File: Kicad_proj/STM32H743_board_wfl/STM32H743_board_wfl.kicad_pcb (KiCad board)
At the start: 4 copper layers, 38.5 x 38.5 mm, 4 parts

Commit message: PCB v0.1b connectors
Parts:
- removed REF** (x4): MountingHole_4mm, MountingHole:MountingHole_4mm
- added C1: 47uF, Capacitor_SMD:C_1206_3216Metric, F.Cu at (192.0, 115.7)
- added C10: 1uF, Capacitor_SMD:C_0603_1608Metric, F.Cu at (191.2, 101.2)
- added C11: 4.7uF, Capacitor_SMD:C_0603_1608Metric, F.Cu at (191.2, 103.7)
- added C12: 4.7uF, Capacitor_SMD:C_0603_1608Metric, F.Cu at (172.1, 114.7)
- added C13: 100nF, Capacitor_SMD:C_0402_1005Metric, F.Cu at (175.5, 121.8)
- added C14: 100nF, Capacitor_SMD:C_0402_1005Metric, F.Cu at (175.5, 123.8)
- added C15: 100nF, Capacitor_SMD:C_0402_1005Metric, F.Cu at (175.5, 125.8)
- added C16: 100nF, Capacitor_SMD:C_0402_1005Metric, F.Cu at (175.5, 127.8)
- added C17: 100nF, Capacitor_SMD:C_0402_1005Metric, F.Cu at (178.4, 121.8)
- added C18: 100nF, Capacitor_SMD:C_0402_1005Metric, F.Cu at (178.4, 123.8)
- added C19: 1uF, Capacitor_SMD:C_0603_1608Metric, F.Cu at (172.1, 117.2)
- added C2: 47uF, Capacitor_SMD:C_1206_3216Metric, F.Cu at (192.0, 119.0)
- added C20: 100nF, Capacitor_SMD:C_0402_1005Metric, F.Cu at (178.4, 125.8)
- added C21: 27pF, Capacitor_SMD:C_0402_1005Metric, F.Cu at (178.4, 127.8)
- added C22: 27pF, Capacitor_SMD:C_0402_1005Metric, F.Cu at (181.2, 121.8)
- added C23: 1uF, Capacitor_SMD:C_0603_1608Metric, F.Cu at (172.1, 119.7)
- added C24: 100nF, Capacitor_SMD:C_0402_1005Metric, F.Cu at (181.2, 123.8)
- added C25: 2.2uF, Capacitor_SMD:C_0603_1608Metric, F.Cu at (172.1, 122.2)
- added C26: 2.2uF, Capacitor_SMD:C_0603_1608Metric, F.Cu at (172.1, 124.7)
- added C27: 1uF, Capacitor_SMD:C_0603_1608Metric, F.Cu at (195.7, 133.2)
- added C28: 100nF, Capacitor_SMD:C_0402_1005Metric, F.Cu at (196.9, 127.9)
- added C29: 100nF, Capacitor_SMD:C_0402_1005Metric, F.Cu at (196.9, 129.8)
- added C3: 1uF, Capacitor_SMD:C_0603_1608Metric, F.Cu at (191.2, 122.0)
- added C30: 100nF, Capacitor_SMD:C_0402_1005Metric, F.Cu at (181.2, 125.8)
- added C31: 100nF, Capacitor_SMD:C_0402_1005Metric, F.Cu at (181.2, 127.8)
- added C4: 100nF, Capacitor_SMD:C_01005_0402Metric, F.Cu at (190.3, 124.0)
- added C5: 10pF, Capacitor_SMD:C_01005_0402Metric, F.Cu at (194.3, 95.7)
- added C6: 1uF, Capacitor_SMD:C_0603_1608Metric, F.Cu at (191.2, 96.2)
- added C7: 47uF, Capacitor_SMD:C_1206_3216Metric, F.Cu at (198.3, 110.3)
- added C8: 10nF, Capacitor_SMD:C_01005_0402Metric, F.Cu at (194.3, 97.4)
- added C9: 4.7uF, Capacitor_SMD:C_0603_1608Metric, F.Cu at (191.2, 98.7)
- added D1: SMBJ26A, Diode_SMD:D_SMB, F.Cu at (142.5, 88.9)
- added F1: 1A Fuse 0680L1000-05, STM32H743_board_library_footprints:FUSC6125X279N, F.Cu at (127.1, 110.0)
- added H1: MountingHole, MountingHole:MountingHole_4mm, F.Cu at (104.0, 104.0)
- added H2: MountingHole, MountingHole:MountingHole_4mm, F.Cu at (104.0, 134.5)
- added H3: MountingHole, MountingHole:MountingHole_4mm, F.Cu at (134.5, 134.5)
- added H4: MountingHole, MountingHole:MountingHole_4mm, F.Cu at (134.5, 104.0)
- added J1: GPS, Connector_JST:JST_GH_SM06B-GHS-TB_1x06-1MP_P1.25mm_Horizontal, F.Cu at (114.3, 135.6)
- added J2: ESC, Connector_JST:JST_GH_SM08B-GHS-TB_1x08-1MP_P1.25mm_Horizontal, F.Cu at (119.1, 103.0)
- added J3: UART, Connector_JST:JST_GH_SM04B-GHS-TB_1x04-1MP_P1.25mm_Horizontal, F.Cu at (125.5, 135.6)
- added J4: Tag_Connect_6pin, Connector:Tag-Connect_TC2030-IDC-NL_2x03_P1.27mm_Vertical, F.Cu at (177.1, 104.0)
- added JP1: PROG_MODE_JUMPER, Resistor_SMD:R_01005_0402Metric, F.Cu at (183.8, 121.7)
- added L1: SPM3020T-2R2M-LR, STM32H743_board_library_footprints:SPM3010-3020, F.Cu at (221.1, 105.9)
- added L3: BLM21PG221SN1D, Inductor_SMD:L_0805_2012Metric, F.Cu at (191.5, 133.4)
- added L4: BLM21PG221SN1D, Inductor_SMD:L_0805_2012Metric, F.Cu at (182.9, 107.9)
- added R1: 100k, Resistor_SMD:R_01005_0402Metric, F.Cu at (194.3, 99.0)
- added R10: 33R, Resistor_SMD:R_01005_0402Metric, F.Cu at (186.1, 123.3)
- added R11: 33R, Resistor_SMD:R_01005_0402Metric, F.Cu at (186.1, 125.0)
- added R12: 33R, Resistor_SMD:R_01005_0402Metric, F.Cu at (186.1, 126.6)
- added R13: 1k, Resistor_SMD:R_01005_0402Metric, F.Cu at (186.1, 128.3)
- added R2: 18.2k, Resistor_SMD:R_01005_0402Metric, F.Cu at (194.3, 100.7)
- added R3: 1M, Resistor_SMD:R_01005_0402Metric, F.Cu at (194.3, 102.3)
- added R4: 182k, Resistor_SMD:R_01005_0402Metric, F.Cu at (194.3, 104.0)
- added R5: 10k, Resistor_SMD:R_01005_0402Metric, F.Cu at (183.8, 123.3)
- added R6: 10k, Resistor_SMD:R_01005_0402Metric, F.Cu at (183.8, 125.0)
- added R7: 4.7k, Resistor_SMD:R_01005_0402Metric, F.Cu at (183.8, 126.6)
- added R8: 4.7k, Resistor_SMD:R_01005_0402Metric, F.Cu at (183.8, 128.3)
- added R9: 33R, Resistor_SMD:R_01005_0402Metric, F.Cu at (186.1, 121.7)
- added U1: LT8609SEV#PBF, STM32H743_board_library_footprints:LT8609SEVPBF, F.Cu at (211.6, 110.5)
- added U2: AP7361C-33E, Package_TO_SOT_SMD:SOT-223-3_TabPin2, F.Cu at (200.4, 99.1)
- added U3: STM32H743VITx, Package_QFP:LQFP-100_14x14mm_P0.5mm, F.Cu at (163.8, 104.2)
- added U4: W25Q512JVEIQ, Package_SON:WSON-8-1EP_6x5mm_P1.27mm_EP3.4x4.3mm, F.Cu at (177.3, 98.2)
- added U5: BMI088, Package_LGA:Bosch_LGA-16_4.5x3mm_P0.5mm_LayoutBorder7x1y_ClockwisePinNumbering, F.Cu at (192.3, 129.6)
- added Y1: 8MHz Crystal, Crystal:Crystal_SMD_Abracon_ABM3-2Pin_5.0x3.2mm, F.Cu at (176.9, 109.1)

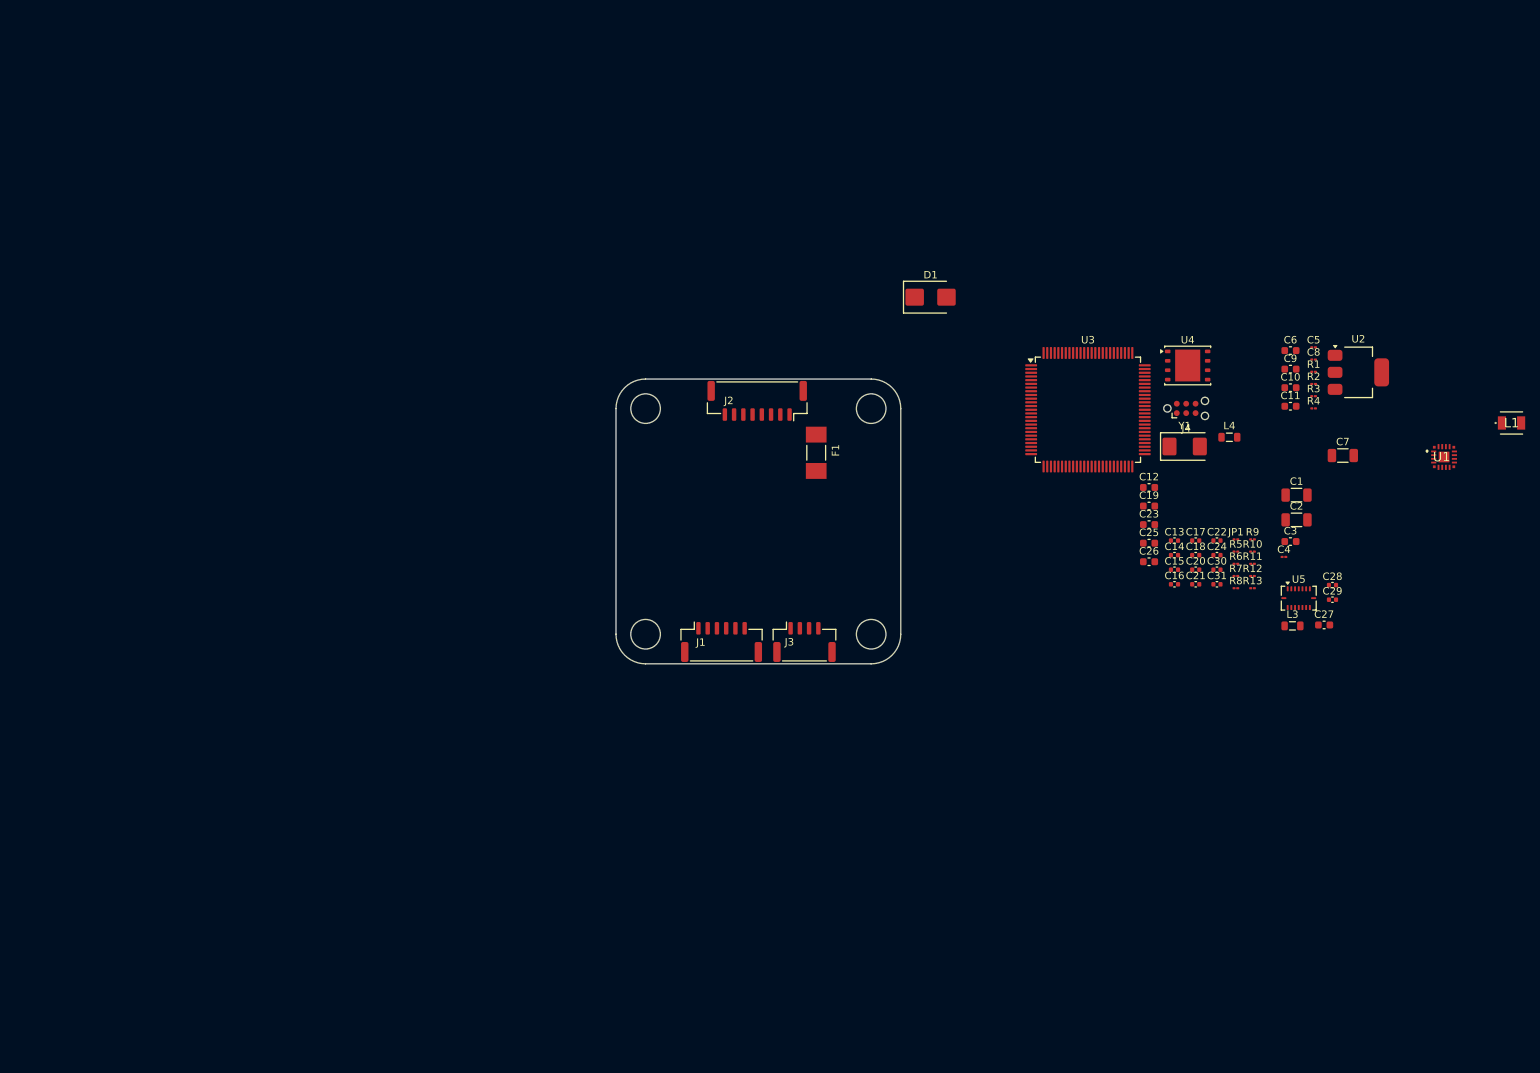
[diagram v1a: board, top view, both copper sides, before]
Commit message: PCB v0.1c components grouping
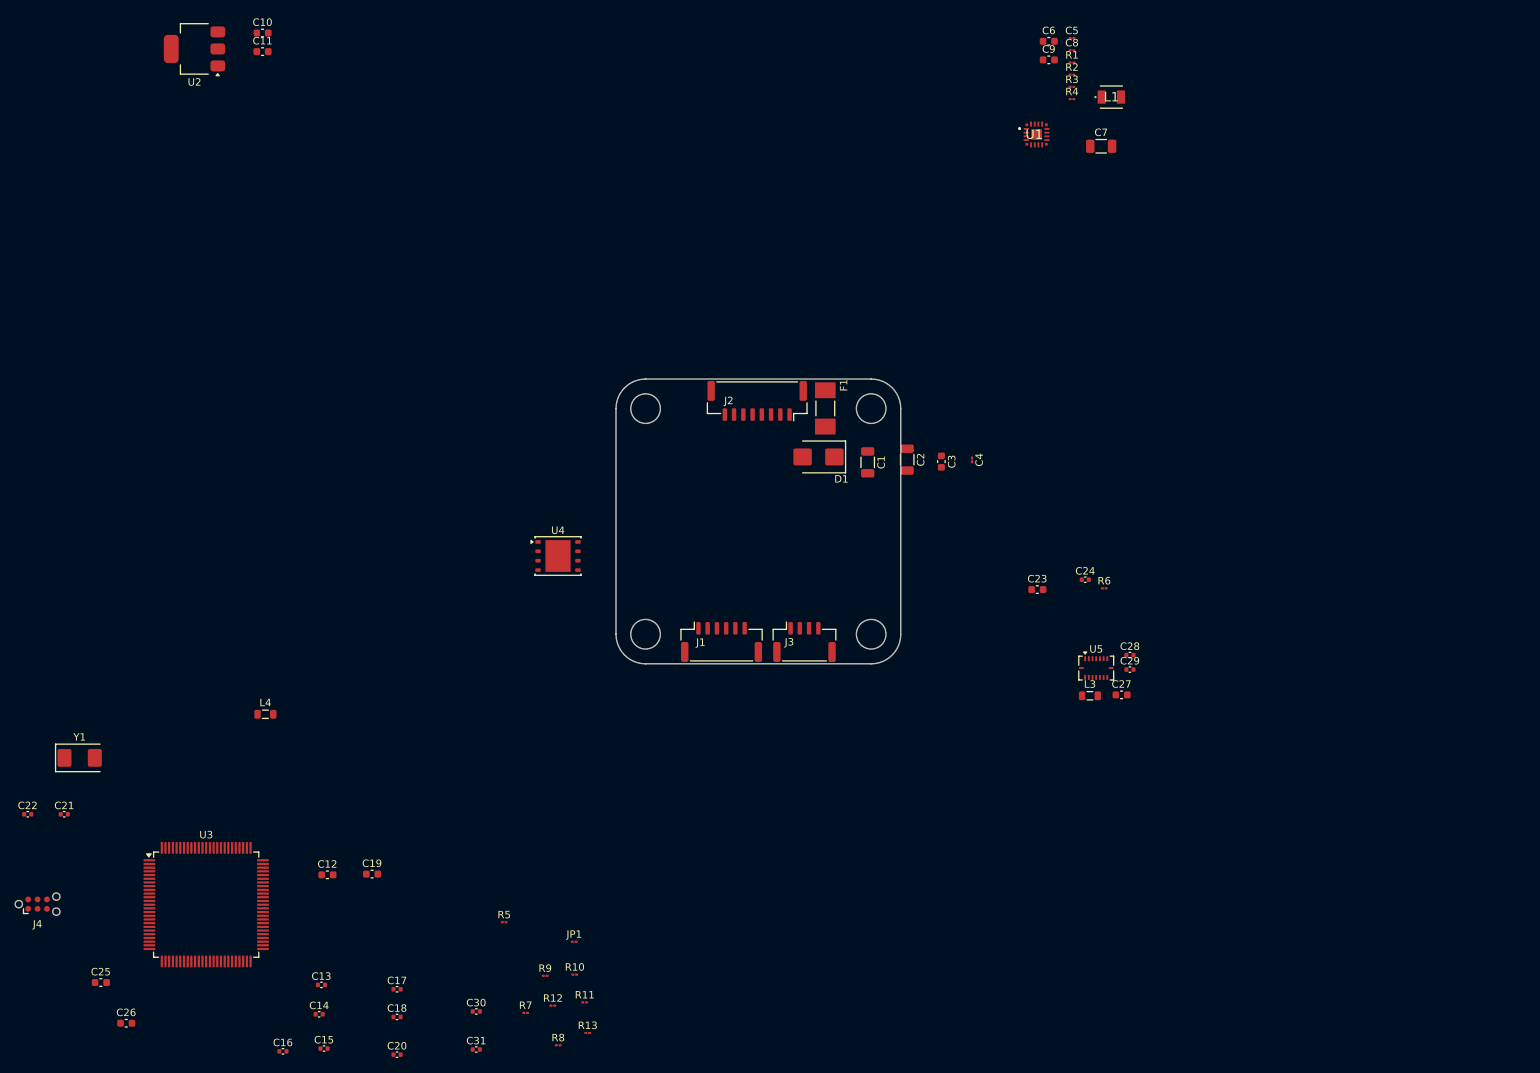
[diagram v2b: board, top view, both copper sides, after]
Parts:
- moved J4 169.1 mm to (21.8, 171.0)
- moved C22 165.0 mm to (20.5, 158.8)
- moved U2 163.3 mm to (43.0, 55.4), turned to 180 degrees
- moved C21 156.1 mm to (25.4, 158.8)
- moved Y1 155.2 mm to (27.5, 151.2)
- moved C25 153.7 mm to (30.4, 181.6)
- moved C26 151.7 mm to (33.8, 187.1)
- moved C10 147.0 mm to (52.2, 53.2)
- moved C11 147.0 mm to (52.2, 55.7)
- moved U3 136.7 mm to (44.6, 171.1)
- moved C16 136.1 mm to (55.0, 190.9)
- moved L4 135.6 mm to (52.6, 145.3)
- moved C15 131.9 mm to (60.5, 190.5)
- moved C14 131.2 mm to (59.9, 185.9)
- moved C13 130.0 mm to (60.2, 181.9)
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
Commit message: PCB v0.1d components placement STM32 caps
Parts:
- removed L4: BLM21PG221SN1D, Inductor_SMD:L_0805_2012Metric
- added L2: BLM21PG221SN1D, Inductor_SMD:L_0805_2012Metric, F.Cu at (42.6, 177.1)
- C21, C22: value 27pF -> 100nF
- C23: value 1uF -> 27pF; footprint Capacitor_SMD:C_0603_1608Metric -> Capacitor_SMD:C_0402_1005Metric
- C24: value 100nF -> 27pF
- C29: value 100nF -> 1uF; footprint Capacitor_SMD:C_0402_1005Metric -> Capacitor_SMD:C_0603_1608Metric
- R13: value 1k -> 10k
- R5: value 10k -> 1k
- moved C30 191.2 mm to (247.1, 90.5)
- moved C31 186.2 mm to (235.6, 86.7)
- moved C23 124.3 mm to (34.0, 110.4)
- moved R6 124.3 mm to (43.1, 110.2)
- moved C24 124.3 mm to (40.5, 109.0)
- moved U5 103.6 mm to (251.0, 81.5)
- moved U4 67.7 mm to (29.3, 98.8)
- moved C20 33.6 mm to (47.6, 166.7), turned to 90 degrees
- moved C16 29.0 mm to (68.0, 164.9), turned to -90 degrees
- moved C22 28.7 mm to (46.0, 172.0), turned to -90 degrees
- moved C17 28.5 mm to (51.8, 160.9)
- moved C18 25.8 mm to (46.8, 175.7), turned to 90 degrees
- moved Y1 24.7 mm to (42.5, 170.8), turned to 90 degrees
- moved C19 24.1 mm to (45.0, 176.8), turned to 90 degrees
- moved C21 23.3 mm to (46.0, 169.7), turned to 90 degrees
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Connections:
- C1 pad 2: -BATT -> GND
- C10 pad 2: -BATT -> GND
- C11 pad 2: -BATT -> GND
- C12 pad 2: -BATT -> GND
- C13 pad 2: -BATT -> GND
- C14 pad 2: -BATT -> GND
- C15 pad 2: -BATT -> GND
- C16 pad 2: -BATT -> GND
- C17 pad 2: -BATT -> GND
- C18 pad 2: -BATT -> GND
- C19 pad 2: -BATT -> GND
- C2 pad 2: -BATT -> GND
- C20 pad 1: /03_STM32H743_schematic/SWD_NRST -> +3V3
- C20 pad 2: -BATT -> GND
- C21 pad 1: Net-(U3-PH0) -> /03_STM32H743_schematic/SWD_NRST
- C21 pad 2: -BATT -> GND
- C22 pad 1: Net-(U3-PH1) -> Net-(U3-PA0)
- C22 pad 2: -BATT -> GND
- C23 pad 1: +3V3 -> Net-(U3-PH0)
- C23 pad 2: -BATT -> GND
- C24 pad 1: +3V3 -> Net-(U3-PH1)
- C24 pad 2: -BATT -> GND
- C25 pad 2: -BATT -> GND
- C26 pad 2: -BATT -> GND
- C27 pad 1: +3V3_IMU -> +3V3
- C27 pad 2: -BATT -> GND
- C28 pad 1: +3V3_IMU -> +3V3
- C28 pad 2: -BATT -> GND
- C29 pad 2: -BATT -> GND
- C3 pad 2: -BATT -> GND
- C30 pad 1: Net-(U3-PA0) -> +3V3_IMU
- C30 pad 2: -BATT -> GND
- C31 pad 1: +3V3 -> +3V3_IMU
- C31 pad 2: -BATT -> GND
- C4 pad 2: -BATT -> GND
- C6 pad 2: -BATT -> GND
- C7 pad 2: -BATT -> GND
- C8 pad 2: -BATT -> GND
- C9 pad 2: -BATT -> GND
- D1 pad 2: -BATT -> GND
- J1 pad 2: -BATT -> GND
- J2 pad 2: -BATT -> GND
- J3 pad 2: -BATT -> GND
- J4 pad 5: -BATT -> GND
- R13 pad 1: /03_STM32H743_schematic/CURRENT -> +3V3
- R13 pad 2: Net-(U3-PA0) -> /03_STM32H743_schematic/FLASH_CS
- R2 pad 2: -BATT -> GND
- R4 pad 2: -BATT -> GND
- R5 pad 1: Net-(JP1-A) -> /03_STM32H743_schematic/CURRENT
- R5 pad 2: -BATT -> Net-(U3-PA0)
- R6 pad 1: +3V3 -> Net-(JP1-A)
- R6 pad 2: /03_STM32H743_schematic/FLASH_CS -> GND
- U1 pad 14: -BATT -> GND
- U1 pad 17: -BATT -> GND
- U1 pad 3: -BATT -> GND
- U1 pad 4: -BATT -> GND
- U1 pad 8: -BATT -> GND
- U2 pad 2: -BATT -> GND
- U3 pad 10: -BATT -> GND
- U3 pad 19: -BATT -> GND
- U3 pad 26: -BATT -> GND
- U3 pad 49: -BATT -> GND
- U3 pad 74: -BATT -> GND
- U3 pad 99: -BATT -> GND
- U4 pad 4: -BATT -> GND
- U4 pad 9: -BATT -> GND
- U5 pad 2: -BATT -> GND
- U5 pad 4: -BATT -> GND
- U5 pad 6: -BATT -> GND
- U5 pad 7: -BATT -> GND
